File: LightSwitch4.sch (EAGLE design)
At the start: 9 parts, among them SW1 SWITCH-SPST-ILLUMINATED, SW2 SWITCH-SPST-ILLUMINATED, SW3 SWITCH-SPST-ILLUMINATED, SW4 SWITCH-SPST-ILLUMINATED

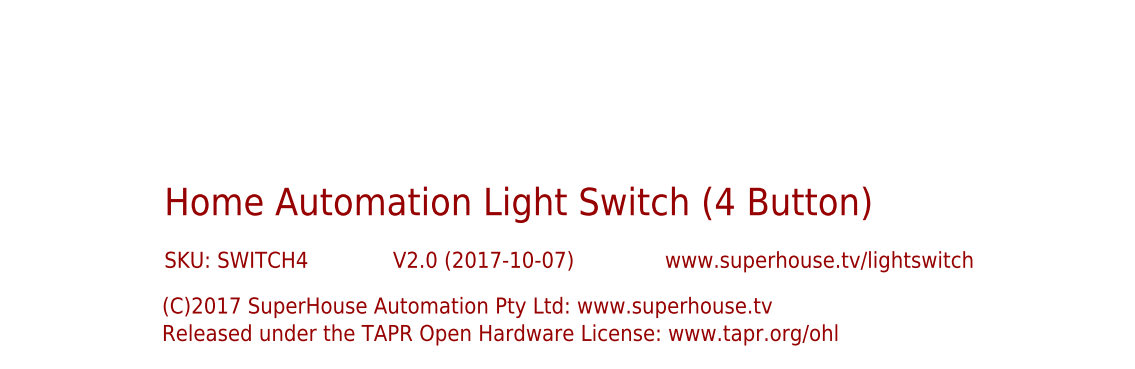
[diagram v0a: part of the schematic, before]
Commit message: Changed button footprint to slotted version for v2.1 release
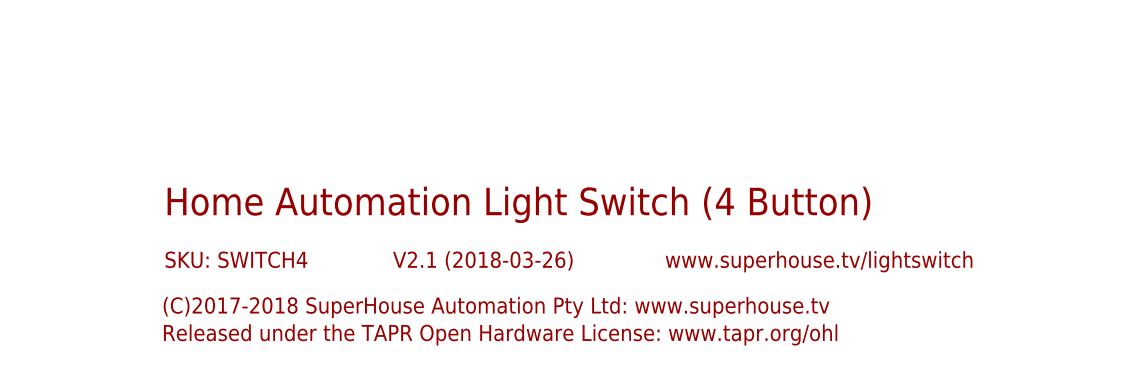
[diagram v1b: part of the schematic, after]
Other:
- note added: "(C)2017-2018 SuperHouse Automation Pty Ltd: www.superhouse.tv"
- note added: "V2.1 (2018-03-26)"
- note removed: "(C)2017 SuperHouse Automation Pty Ltd: www.superhouse.tv"
- note removed: "V2.0 (2017-10-07)"
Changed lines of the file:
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@@
 <?xml version="1.0" encoding="utf-8"?>
 <!DOCTYPE eagle SYSTEM "eagle.dtd">
-<eagle version="8.3.2">
+<eagle version="8.7.0">
 <drawing>
 <settings>
-<setting alwaysvectorfont="yes"/>
+<setting alwaysvectorfont="no"/>
 <setting keepoldvectorfont="yes"/>
 <setting verticaltext="up"/>
@@
 <layer number="60" name="p_dimension" color="6" fill="0" visible="no" active="no"/>
 <layer number="61" name="pt_docu" color="7" fill="0" visible="no" active="no"/>
+<layer number="88" name="SimResults" color="9" fill="1" visible="yes" active="yes"/>
+<layer number="89" name="SimProbes" color="9" fill="1" visible="yes" active="yes"/>
 <layer number="90" name="Modules" color="7" fill="1" visible="yes" active="yes"/>
 <layer number="91" name="Nets" color="2" fill="1" visible="yes" active="yes"/>
@@
 <text x="48.26" y="104.14" size="1.778" layer="97">GND</text>
 <text x="139.7" y="20.32" size="3.048" layer="94">Home Automation Light Switch (4 Button)</text>
-<text x="165.1" y="14.478" size="1.778" layer="94">V2.0 (2017-10-07)</text>
+<text x="165.1" y="14.478" size="1.778" layer="94">V2.1 (2018-03-26)</text>
 <text x="139.7" y="14.478" size="1.778" layer="94">SKU: SWITCH4</text>
-<text x="139.446" y="9.398" size="1.778" layer="94">(C)2017 SuperHouse Automation Pty Ltd: www.superhouse.tv</text>
+<text x="139.446" y="9.398" size="1.778" layer="94">(C)2017-2018 SuperHouse Automation Pty Ltd: www.superhouse.tv</text>
 <text x="139.446" y="6.35" size="1.778" layer="94">Released under the TAPR Open Hardware License: www.tapr.org/ohl</text>
 <text x="195.326" y="14.478" size="1.778" layer="94">www.superhouse.tv/lightswitch</text>

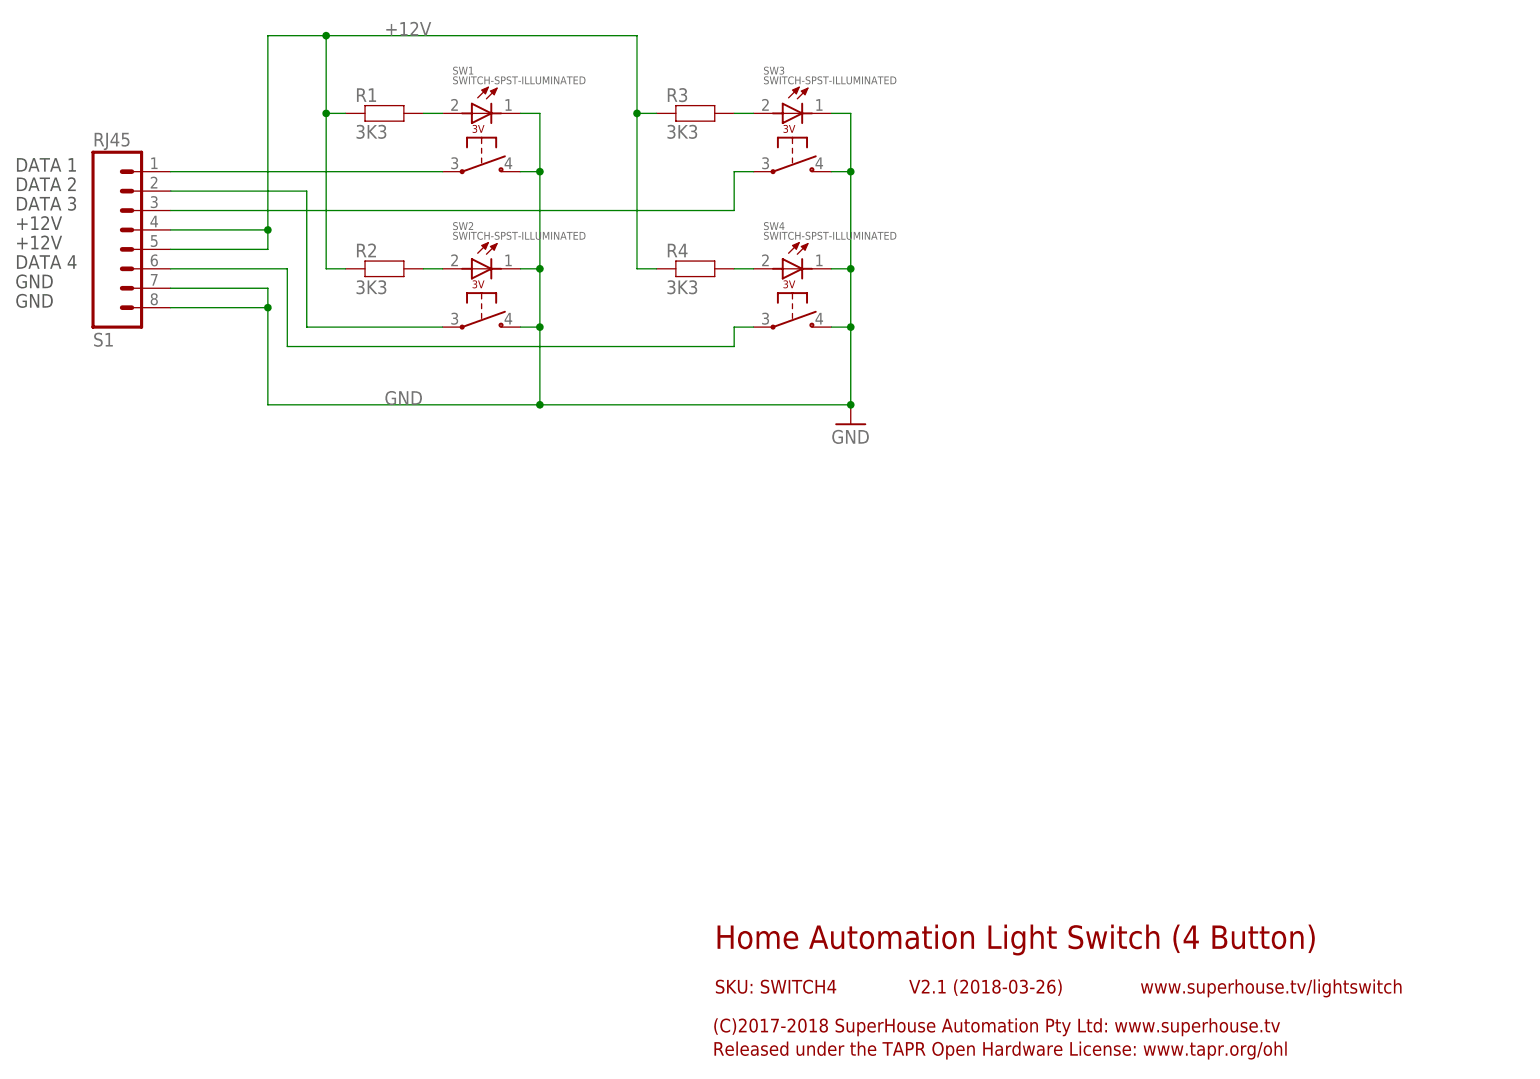
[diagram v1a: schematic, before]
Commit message: Updated RJ45 footprint for v2.2
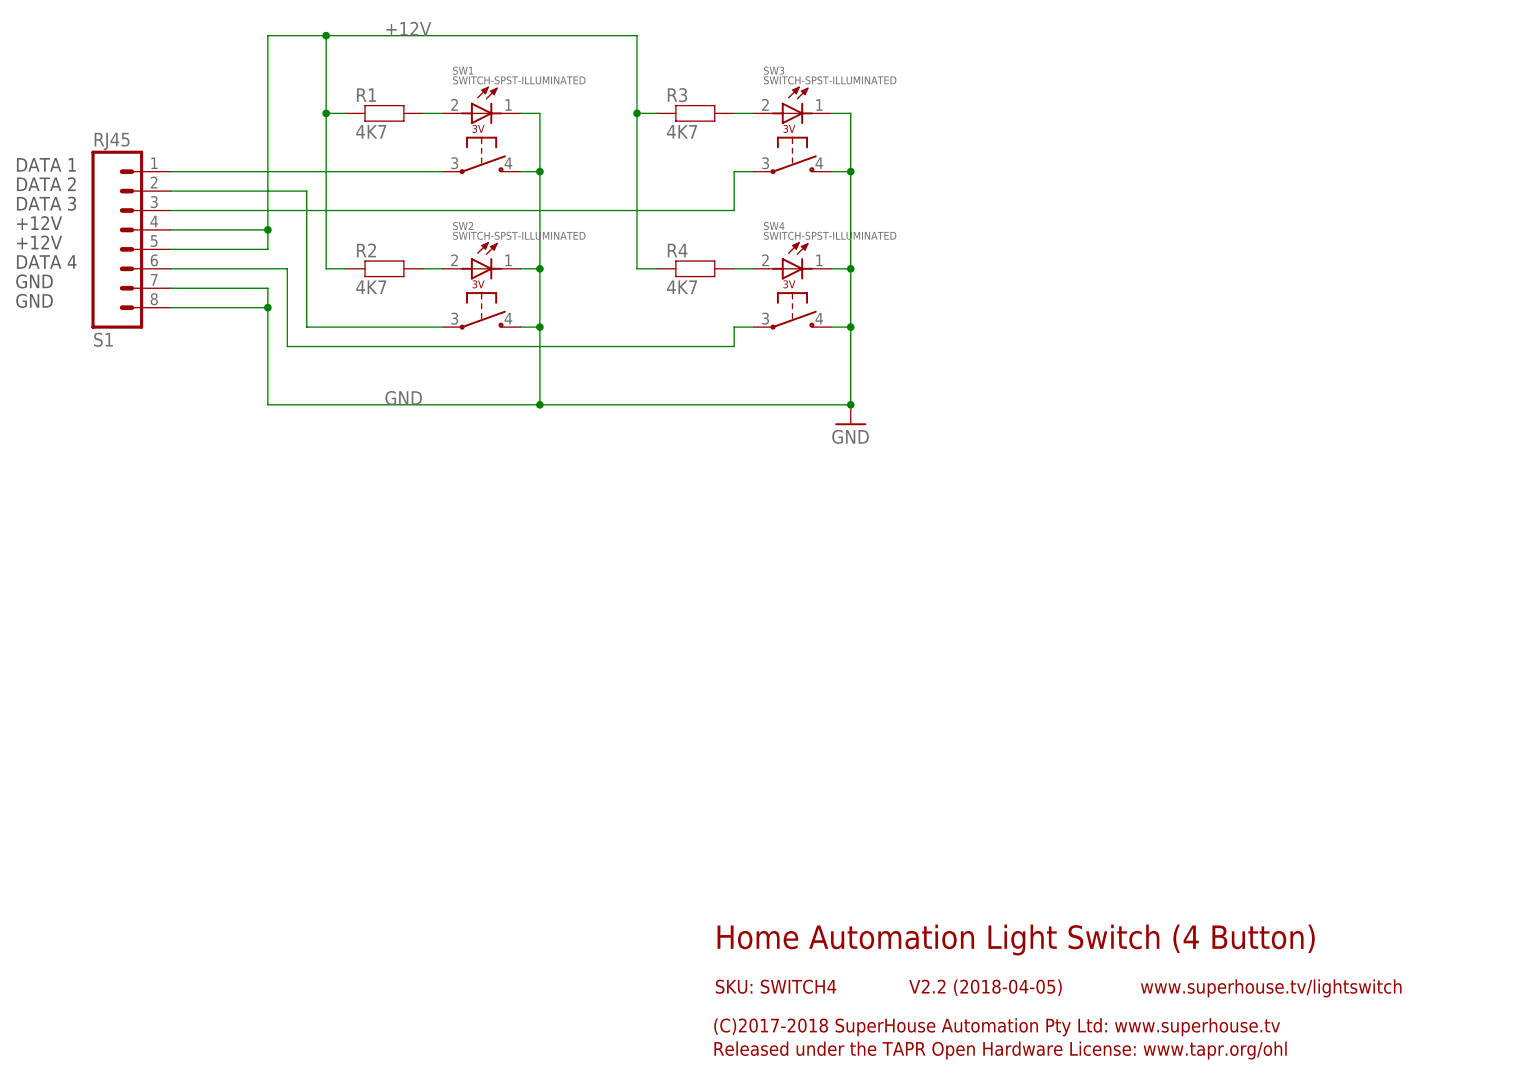
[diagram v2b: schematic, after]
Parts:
- R1, R2, R3, R4: value 3K3 -> 4K7
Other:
- note added: "V2.2 (2018-04-05)"
- note removed: "V2.1 (2018-03-26)"
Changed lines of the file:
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@@
 <part name="SW3" library="freetronics-jon" deviceset="SWITCH-SPST-ILLUMINATED" device=""/>
 <part name="SW4" library="freetronics-jon" deviceset="SWITCH-SPST-ILLUMINATED" device=""/>
-<part name="R1" library="freetronics-jon" deviceset="RESISTOR" device="0603" value="3K3"/>
-<part name="R2" library="freetronics-jon" deviceset="RESISTOR" device="0603" value="3K3"/>
-<part name="R3" library="freetronics-jon" deviceset="RESISTOR" device="0603" value="3K3"/>
-<part name="R4" library="freetronics-jon" deviceset="RESISTOR" device="0603" value="3K3"/>
+<part name="R1" library="freetronics-jon" deviceset="RESISTOR" device="0603" value="4K7"/>
+<part name="R2" library="freetronics-jon" deviceset="RESISTOR" device="0603" value="4K7"/>
+<part name="R3" library="freetronics-jon" deviceset="RESISTOR" device="0603" value="4K7"/>
+<part name="R4" library="freetronics-jon" deviceset="RESISTOR" device="0603" value="4K7"/>
 </parts>
 <sheets>
@@
 <text x="48.26" y="104.14" size="1.778" layer="97">GND</text>
 <text x="139.7" y="20.32" size="3.048" layer="94">Home Automation Light Switch (4 Button)</text>
-<text x="165.1" y="14.478" size="1.778" layer="94">V2.1 (2018-03-26)</text>
+<text x="165.1" y="14.478" size="1.778" layer="94">V2.2 (2018-04-05)</text>
 <text x="139.7" y="14.478" size="1.778" layer="94">SKU: SWITCH4</text>
 <text x="139.446" y="9.398" size="1.778" layer="94">(C)2017-2018 SuperHouse Automation Pty Ltd: www.superhouse.tv</text>

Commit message: Release v2.2
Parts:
- S1: value RJ45 -> RJ45JC; device freetronics-jon:RJ45 -> freetronics-jon:RJ45JC
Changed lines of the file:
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@@
 <?xml version="1.0" encoding="utf-8"?>
 <!DOCTYPE eagle SYSTEM "eagle.dtd">
-<eagle version="8.7.0">
+<eagle version="9.2.1">
 <drawing>
 <settings>
@@
 <parts>
 <part name="GND3" library="SparkFun" deviceset="GND" device=""/>
-<part name="S1" library="freetronics-jon" deviceset="RJ45" device=""/>
+<part name="S1" library="freetronics-jon" deviceset="RJ45" device="JC"/>
 <part name="SW1" library="freetronics-jon" deviceset="SWITCH-SPST-ILLUMINATED" device=""/>
 <part name="SW2" library="freetronics-jon" deviceset="SWITCH-SPST-ILLUMINATED" device=""/>
@@
 </plain>
 <instances>
-<instance part="GND3" gate="1" x="157.48" y="88.9"/>
-<instance part="S1" gate="G$1" x="60.96" y="111.76" rot="MR180"/>
-<instance part="SW1" gate="G$1" x="109.22" y="121.92"/>
-<instance part="SW2" gate="G$1" x="109.22" y="101.6"/>
-<instance part="SW3" gate="G$1" x="149.86" y="121.92"/>
-<instance part="SW4" gate="G$1" x="149.86" y="101.6"/>
-<instance part="R1" gate="G$1" x="96.52" y="129.54"/>
-<instance part="R2" gate="G$1" x="96.52" y="109.22"/>
-<instance part="R3" gate="G$1" x="137.16" y="129.54"/>
-<instance part="R4" gate="G$1" x="137.16" y="109.22"/>
+<instance part="GND3" gate="1" x="157.48" y="88.9" smashed="yes">
+<attribute name="VALUE" x="154.94" y="86.36" size="1.778" layer="96"/>
+</instance>
+<instance part="S1" gate="G$1" x="60.96" y="111.76" smashed="yes" rot="MR180">
+<attribute name="VALUE" x="58.42" y="127" size="1.778" layer="96" rot="MR180"/>
+<attribute name="NAME" x="58.42" y="100.838" size="1.778" layer="95" rot="MR180"/>
+</instance>
+<instance part="SW1" gate="G$1" x="109.22" y="121.92" smashed="yes">
+<attribute name="NAME" x="105.41" y="134.62" size="1.016" layer="95"/>
+<attribute name="VALUE" x="105.41" y="133.35" size="1.016" layer="96"/>
+</instance>
+<instance part="SW2" gate="G$1" x="109.22" y="101.6" smashed="yes">
+<attribute name="NAME" x="105.41" y="114.3" size="1.016" layer="95"/>
+<attribute name="VALUE" x="105.41" y="113.03" size="1.016" layer="96"/>
+</instance>
+<instance part="SW3" gate="G$1" x="149.86" y="121.92" smashed="yes">
+<attribute name="NAME" x="146.05" y="134.62" size="1.016" layer="95"/>
+<attribute name="VALUE" x="146.05" y="133.35" size="1.016" layer="96"/>
+</instance>
+<instance part="SW4" gate="G$1" x="149.86" y="101.6" smashed="yes">
+<attribute name="NAME" x="146.05" y="114.3" size="1.016" layer="95"/>
+<attribute name="VALUE" x="146.05" y="113.03" size="1.016" layer="96"/>
+</instance>
+<instance part="R1" gate="G$1" x="96.52" y="129.54" smashed="yes">
+<attribute name="NAME" x="92.71" y="131.0386" size="1.778" layer="95"/>
+<attribute name="VALUE" x="92.71" y="126.238" size="1.778" layer="96"/>
+</instance>
+<instance part="R2" gate="G$1" x="96.52" y="109.22" smashed="yes">
+<attribute name="NAME" x="92.71" y="110.7186" size="1.778" layer="95"/>
+<attribute name="VALUE" x="92.71" y="105.918" size="1.778" layer="96"/>
+</instance>
+<instance part="R3" gate="G$1" x="137.16" y="129.54" smashed="yes">
+<attribute name="NAME" x="133.35" y="131.0386" size="1.778" layer="95"/>
+<attribute name="VALUE" x="133.35" y="126.238" size="1.778" layer="96"/>
+</instance>
+<instance part="R4" gate="G$1" x="137.16" y="109.22" smashed="yes">
+<attribute name="NAME" x="133.35" y="110.7186" size="1.778" layer="95"/>
+<attribute name="VALUE" x="133.35" y="105.918" size="1.778" layer="96"/>
+</instance>
 </instances>
 <busses>
